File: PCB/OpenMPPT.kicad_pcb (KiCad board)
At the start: 2 copper layers, 77 x 47 mm, 41 parts, among them J101 THERM, J103 XT60, J104 XT60, Q101 FDMS8050, Q102 FDMS8050, Q103 FDMS8050, Q104 FDMS8050, U101 BQ24650

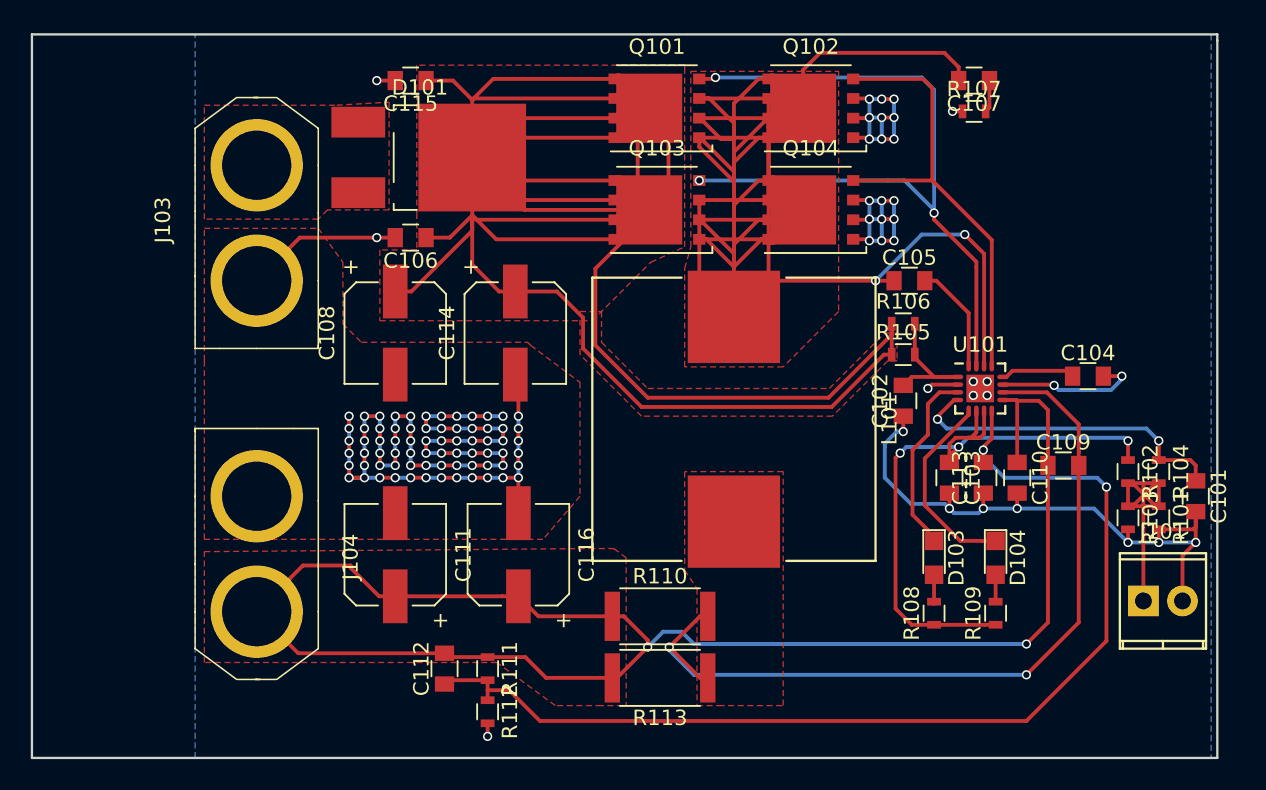
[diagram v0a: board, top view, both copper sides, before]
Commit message: Add MPPT resistors
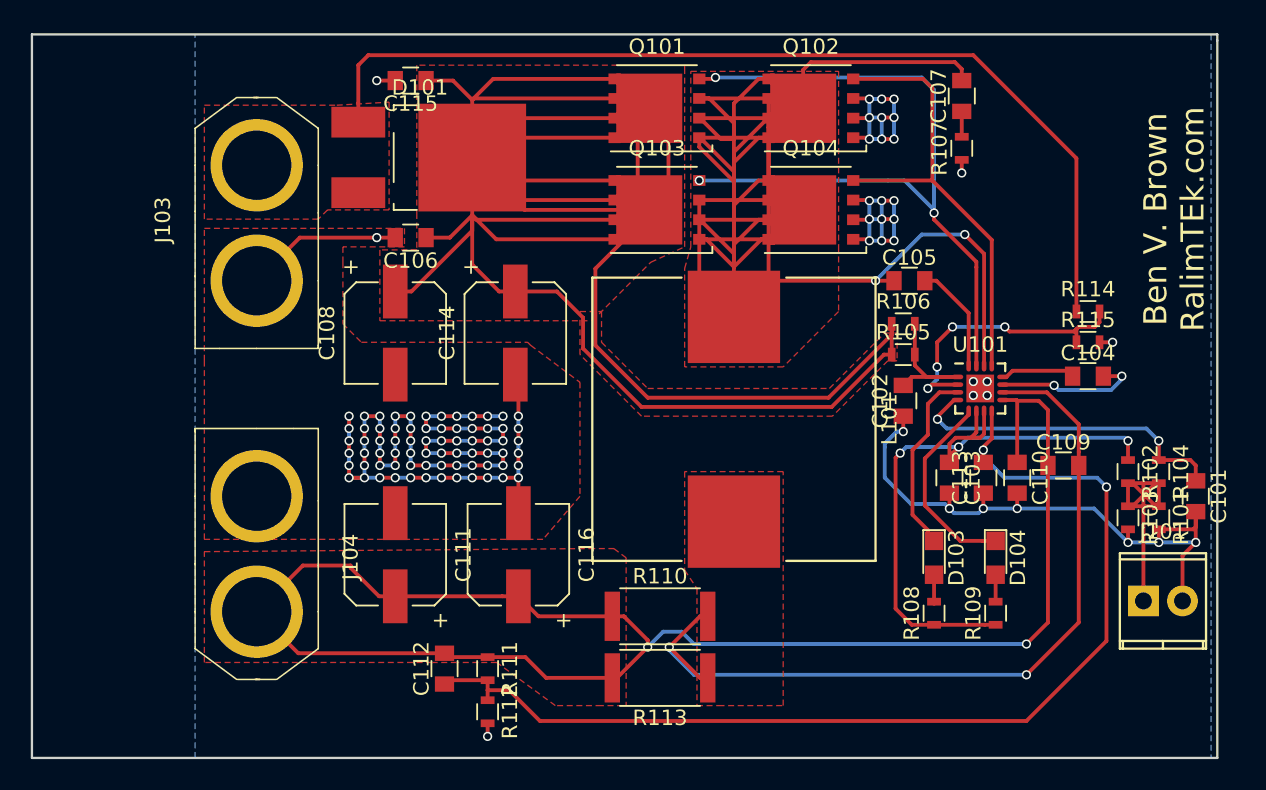
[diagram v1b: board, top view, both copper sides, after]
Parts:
- added R114: 499k, Resistors_SMD:R_0603, F.Cu at (152.0, 88.0)
- added R115: 36k, Resistors_SMD:R_0603, F.Cu at (152.0, 90.0)
- moved R107 2.53 mm to (143.8, 77.4), turned to 90 degrees
- moved C107 1.28 mm to (143.8, 74.0), turned to 90 degrees
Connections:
- U101 pad 2: (no net) -> /MPPTSET
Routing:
- net Net-(D101-Pad1): track 0.00 -> 63.3 mm
- net /MPPTSET: track 0.00 -> 18.2 mm, vias 0 -> 4
- net (no net): track 2.03 -> 0.00 mm, vias 1 -> 0
- net GND: track 164.8 -> 165.9 mm, vias 107 -> 108
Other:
- board text added: "Ben V. Brown RalimTEk.com"

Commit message: Finish Routing
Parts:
- removed R104: 100, Resistors_SMD:R_0603
- removed R107: -, Resistors_SMD:R_0603
- added D102: D_Schottky, Diodes_SMD:D_SOD-523, F.Cu at (152.0, 89.4)
- C107: value - -> 1.0uF
- J103, J104: footprint xt60:XT60 -> xt60:XT30PW_Male
- R105: value 10 -> -
- R108, R109: value R -> 5.23k
- moved C107 22.5 mm to (153.6, 94.2), turned to 0 degrees
- moved J103 8.14 mm to (90.0, 80.0), turned to 0 degrees
- moved J104 8.14 mm to (90.0, 106.0), turned to 0 degrees
- moved R114 2.40 mm to (152.0, 85.6)
- moved R115 2.40 mm to (152.0, 87.6)
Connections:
- C107 pad 1: Net-(C107-Pad1) -> Net-(C104-Pad1)
- C107 pad 2: Net-(C105-Pad1) -> GND
- J101 pad 1: Net-(J101-Pad1) -> Net-(C101-Pad1)
- R101 pad 1: Net-(J101-Pad1) -> Net-(C101-Pad1)
- R102 pad 2: Net-(J101-Pad1) -> Net-(C101-Pad1)
- R103 pad 1: Net-(J101-Pad1) -> Net-(C101-Pad1)
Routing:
- net (no net): track 0.00 -> 65.6 mm, vias 0 -> 72
- net GND: track 165.9 -> 107.5 mm, vias 108 -> 42
- net Net-(C101-Pad1): track 21.7 -> 43.1 mm
- net Net-(J101-Pad1): track 19.9 -> 0.00 mm
- net Net-(C109-Pad1): track 105.5 -> 87.3 mm
- net Net-(C105-Pad2): track 7.14 -> 15.7 mm, vias 0 -> 2
- net Net-(C105-Pad1): track 188.5 -> 181.4 mm
- net Net-(C104-Pad1): track 4.84 -> 11.4 mm
- net Net-(D101-Pad1): track 63.3 -> 60.9 mm
- net Net-(C107-Pad1): track 1.65 -> 0.00 mm
- net /MPPTSET: track 18.2 -> 19.5 mm
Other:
- board size 77 x 47 mm -> 74.8 x 47 mm
- net class Default: via_dia 0.6 -> 0.9; via_drill 0.4 -> 0.5
- rule via_min_size: 0.4 -> 0.8
- board text added: "OpenMPPT"
